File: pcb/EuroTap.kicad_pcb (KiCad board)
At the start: 2 copper layers, 34 x 17 mm, 5 parts, among them J1 AudioJack3_Ground, J2 AudioJack3_Ground, J3 Conn_Coaxial

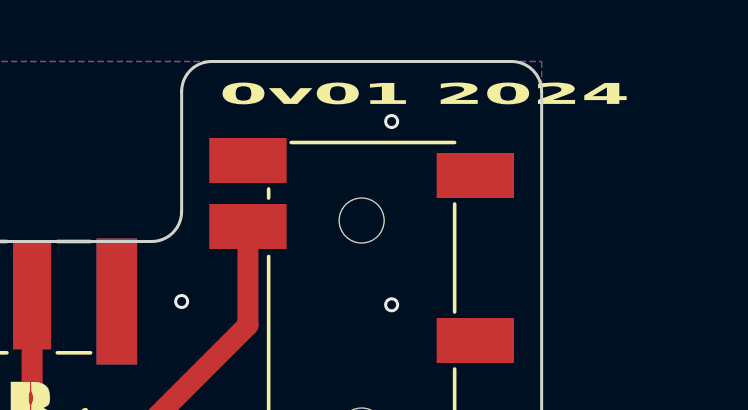
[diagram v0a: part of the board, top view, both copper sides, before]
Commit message: Add teardrops
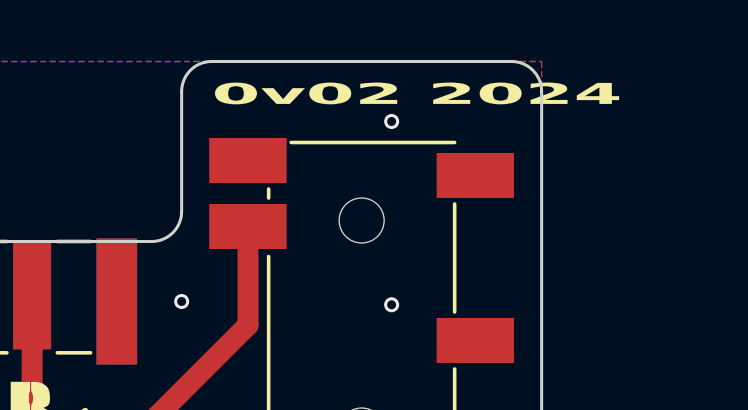
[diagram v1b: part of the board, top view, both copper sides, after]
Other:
- board text added: "0v02 2024"
- board text removed: "0v01 2024"

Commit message: 30cm width
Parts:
- removed the Ref** at (137.4, 116.7)
- added Ref**: Val**, SloBloLogo, F.Cu at (137.8, 117.5)
- J1, J2: footprint SloBlo:Jack_3.5mm_PJ311_Horizontal_Handsolder -> SloBlo:Jack_3.5mm_PJ311_Horizontal
- moved J1 1.00 mm to (145.0, 108.0)
- moved J2 1.00 mm to (125.0, 108.0)
- moved J3 1.00 mm to (135.0, 109.0)
- moved G*** 0.42 mm to (135.0, 108.5)
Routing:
- net /Signal: track 36.6 -> 34.5 mm
- net GND: vias 11 -> 10
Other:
- board size 34 x 17 mm -> 30 x 17 mm
- board text added: "2024"
- board text removed: "0v02 2024"
